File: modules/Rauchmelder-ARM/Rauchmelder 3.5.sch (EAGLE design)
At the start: 61 parts, among them IC2 LPC1115, IC3 BD9G101, Q1 BC856, Q3 BCP52, Q4 ASFL, T1 BC848

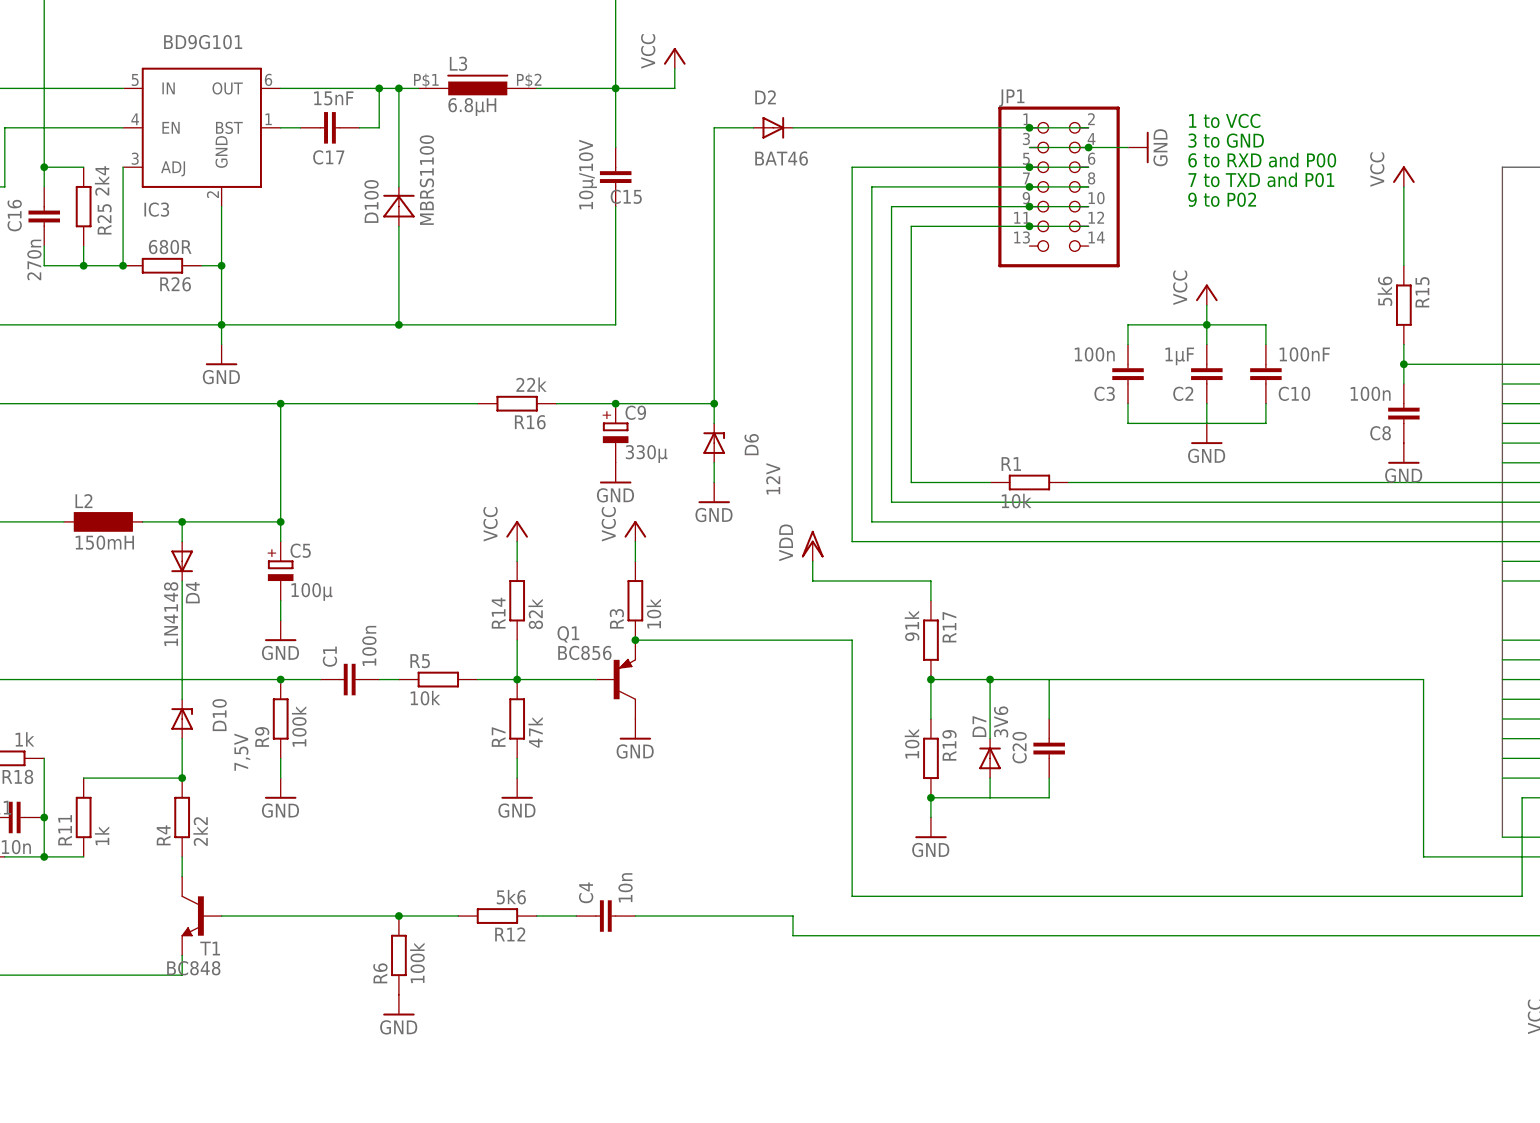
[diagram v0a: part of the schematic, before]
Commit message: Fix a few part values in Rauchmelder_3.5
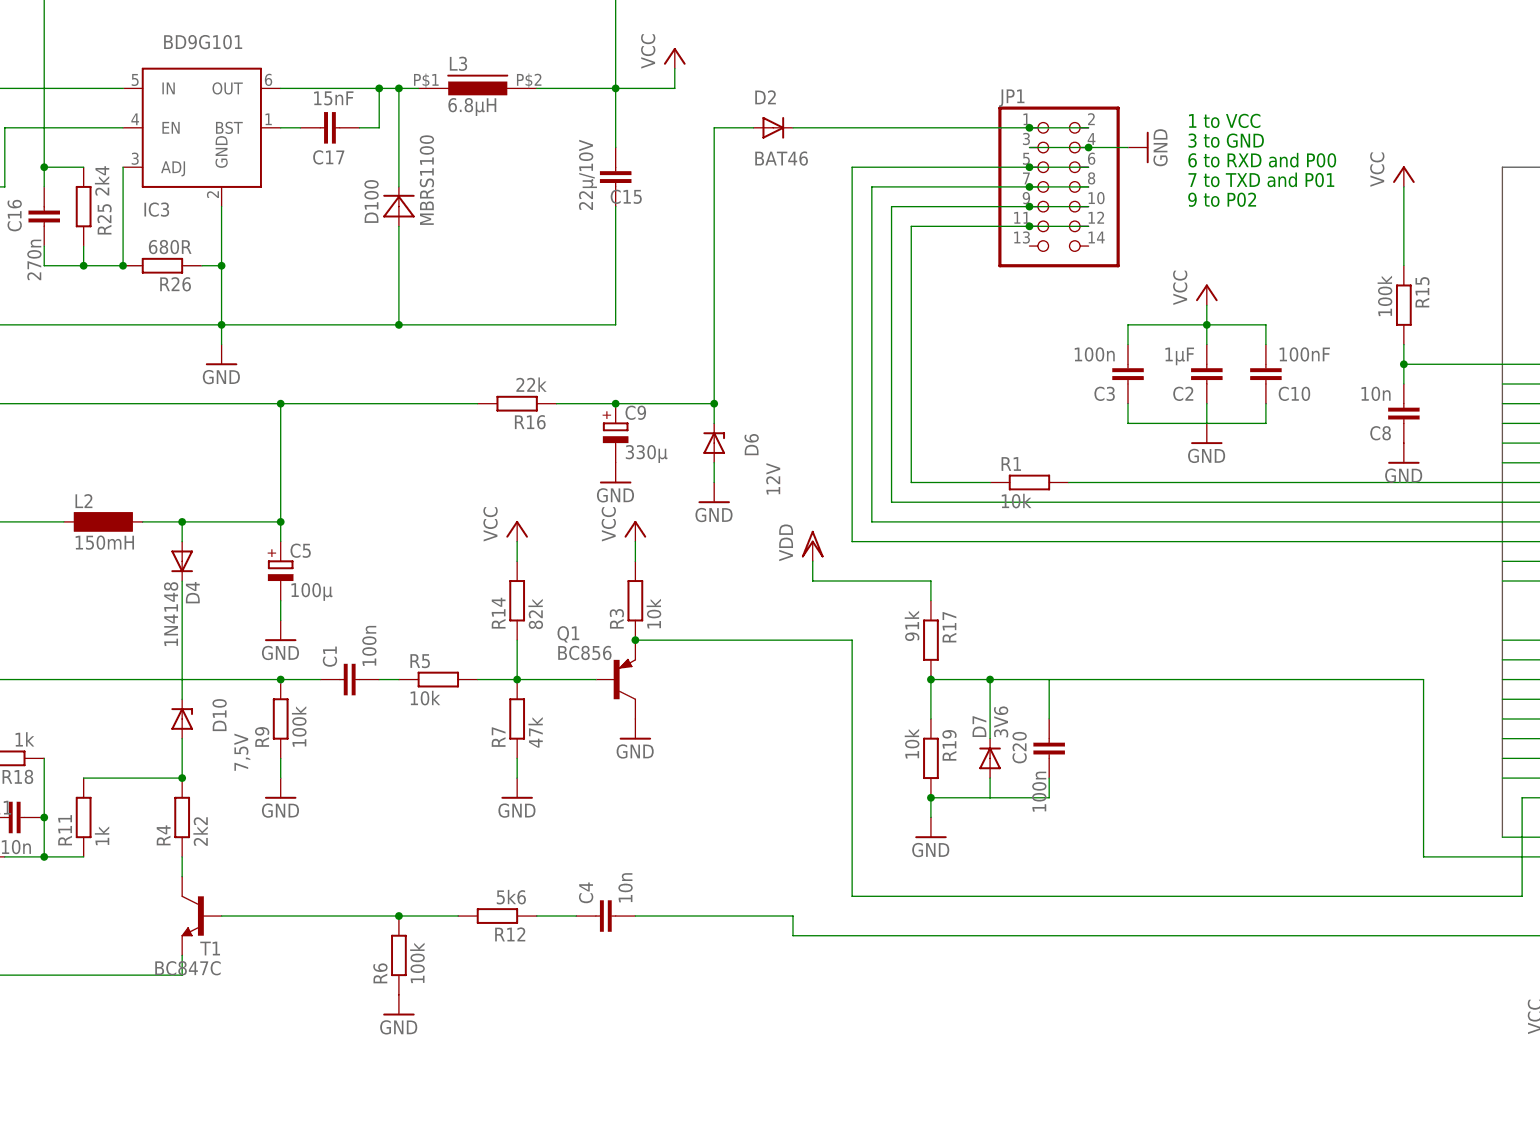
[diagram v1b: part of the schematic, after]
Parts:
- C15: value 10µ/10V -> 22µ/10V
- C20: value (none) -> 100n
- C8: value 100n -> 10n
- R15: value 5k6 -> 100k
- T1: value BC848 -> BC847C; device transistor:BC848 -> transistor:BC847C
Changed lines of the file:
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@@
 <part name="C11" library="rcl" deviceset="C-EU" device="C1206" value="10n"/>
 <part name="D5" library="diode" deviceset="SUPPRESSOR-" device="SMBJ" value="SMAJ40"/>
-<part name="C8" library="rcl" deviceset="C-EU" device="C1206" value="100n"/>
-<part name="R15" library="rcl" deviceset="R-EU_" device="R1206" value="5k6"/>
+<part name="C8" library="rcl" deviceset="C-EU" device="C1206" value="10n"/>
+<part name="R15" library="rcl" deviceset="R-EU_" device="R1206" value="100k"/>
 <part name="GND3" library="supply1" deviceset="GND" device=""/>
 <part name="P+5" library="supply1" deviceset="VCC" device=""/>
@@
 <part name="Q3" library="transistor-pnp" deviceset="FZT753SMD" device="" value="BCP52"/>
 <part name="Q1" library="transistor-pnp" deviceset="BC856*" device="SMD" technology="ALT1" value="BC856"/>
-<part name="T1" library="transistor" deviceset="BC848" device=""/>
+<part name="T1" library="transistor" deviceset="BC847C" device=""/>
 <part name="D10" library="diode" deviceset="ZPD" device="" value="7,5V"/>
 <part name="D6" library="diode" deviceset="ZPD" device="" value="12V"/>
@@
 <part name="R19" library="rcl" deviceset="R-EU_" device="R1206" value="10k"/>
 <part name="D7" library="diode" deviceset="DIODE-" device="MINIMELF" value="3V6"/>
-<part name="C20" library="rcl" deviceset="C-EU" device="C1206"/>
+<part name="C20" library="rcl" deviceset="C-EU" device="C1206" value="100n"/>
 <part name="VDD1" library="supply1" deviceset="VDD" device=""/>
 <part name="GND18" library="supply1" deviceset="GND" device=""/>
@@
 <part name="L3" library="Stefan_selfbus" deviceset="IND_FASTRON_1616FPS" device="" value="6.8µH"/>
 <part name="C7" library="rcl" deviceset="C-EU" device="C1206K" value="4.7µF/50V"/>
-<part name="C15" library="rcl" deviceset="C-EU" device="C1206" value="10µ/10V"/>
+<part name="C15" library="rcl" deviceset="C-EU" device="C1206" value="22µ/10V"/>
 <part name="R23" library="rcl" deviceset="R-EU_" device="R1206" value="NC"/>
 <part name="R24" library="rcl" deviceset="R-EU_" device="R1206" value="0R"/>
